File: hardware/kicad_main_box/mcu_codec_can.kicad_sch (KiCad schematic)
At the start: 0 parts

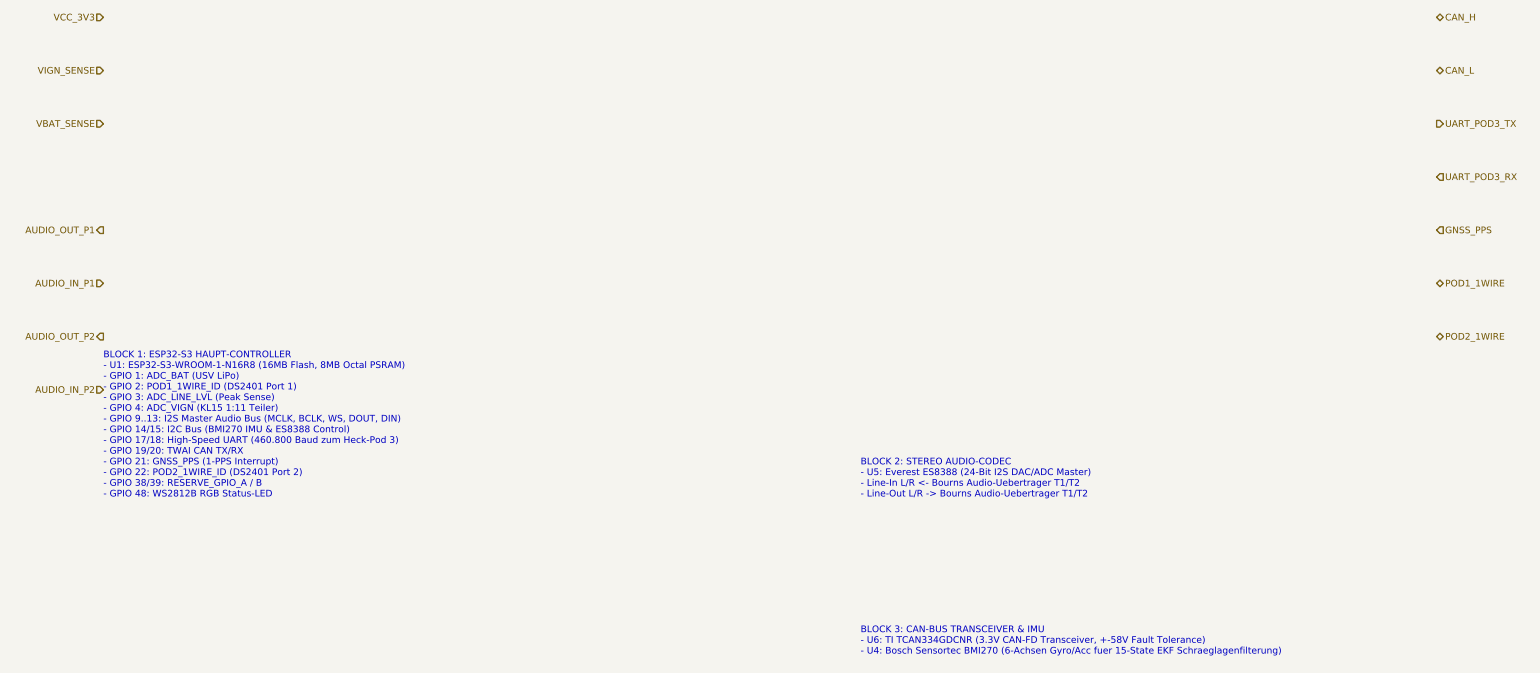
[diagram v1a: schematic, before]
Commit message: feat(kicad): Implement full graphical electronic schematic drawings (symbols, pins, wires, components) for all boards
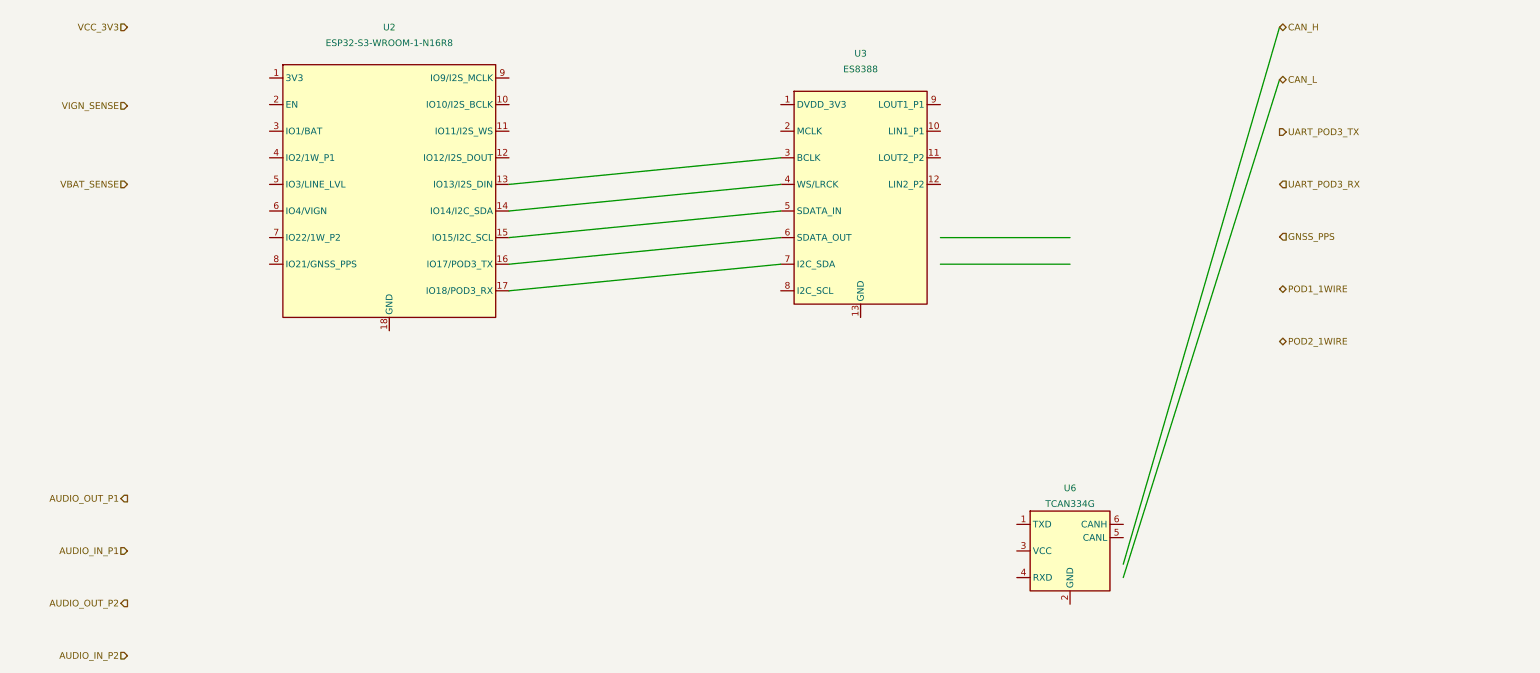
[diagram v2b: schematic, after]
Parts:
- added U2: ESP32-S3-WROOM-1-N16R8, symbol RF_Module:ESP32-S3-WROOM-1
- added U3: ES8388, symbol Audio:ES8388
- added U6: TCAN334G, symbol Interface_CAN_LIN:TCAN334G
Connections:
- new net: U2.13 (IO13/I2S_DIN), U3.3 (BCLK)
- new net: U2.14 (IO14/I2C_SDA), U3.4 (WS/LRCK)
- new net: U2.15 (IO15/I2C_SCL), U3.5 (SDATA_IN)
- new net: U2.16 (IO17/POD3_TX), U3.6 (SDATA_OUT)
- new net: U2.17 (IO18/POD3_RX), U3.7 (I2C_SDA)
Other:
- note removed: "BLOCK 1: ESP32-S3 HAUPT-CONTROLLER - U1: ESP32-S3-WROOM-1-N16R8 (16MB Flash, 8MB Octal PSRAM) - GPIO 1: ADC_BAT (USV LiPo) - GPIO 2: POD1_1WIRE_ID (DS2401 Port 1) - GPIO 3: ADC_LINE_LVL (Peak Sense) - GPIO 4: ADC_VIGN (KL15 1:11 Teiler) - GPIO 9..13: I2S Master Audio Bus (MCLK, BCLK, WS, DOUT, DIN) - GPIO 14/15: I2C Bus (BMI270 IMU & ES8388 Control) - GPIO 17/18: High-Speed UART (460.800 Baud zum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"
- note removed: "BLOCK 2: STEREO AUDIO-CODEC - U5: Everest ES8388 (24-Bit I2S DAC/ADC Master) - Line-In L/R <- Bourns Audio-Uebertrager T1/T2 - Line-Out L/R -> Bourns Audio-Uebertrager T1/T2"
- note removed: "BLOCK 3: CAN-BUS TRANSCEIVER & IMU - U6: TI TCAN334GDCNR (3.3V CAN-FD Transceiver, +-58V Fault Tolerance) - U4: Bosch Sensortec BMI270 (6-Achsen Gyro/Acc fuer 15-State EKF Schraeglagenfilterung)"
- company: (none) -> OpenMotorBridge Open Source Hardware
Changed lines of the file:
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@@
-(kicad_sch (version 20260206) (generator "eeschema") (generator_version "10.0")
-  (paper "A3")
-  (title_block
-    (title "OpenMotorBridge v8.0 - MCU, Audio Codec & CAN-Bus")
-    (date "2026-08-23")
-    (rev "v8.0")
-    (comment 1 "ESP32-S3-WROOM-1-N16R8 Dual-Core MCU (240 MHz)")
-    (comment 2 "Everest ES8388 24-Bit I2S Codec + TI TCAN334G CAN-FD + Bosch BMI270 IMU")
-  )
-  (hierarchical_label "VCC_3V3" (shape input) (at 25.4 38.1 180)
-    (effects (font (size 1.27 1.27)) (justify right))
-  )
-  (hierarchical_label "VIGN_SENSE" (shape input) (at 25.4 48.26 180)
-    (effects (font (size 1.27 1.27)) (justify right))
-  )
-  (hierarchical_label "VBAT_SENSE" (shape input) (at 25.4 58.42 180)
-    (effects (font (size 1.27 1.27)) (justify right))
-  )
-  (hierarchical_label "CAN_H" (shape bidirectional) (at 280.0 38.1 0)
-    (effects (font (size 1.27 1.27)) (justify left))
-  )
-  (hierarchical_label "CAN_L" (shape bidirectional) (at 280.0 48.26 0)
-    (effects (font (size 1.27 1.27)) (justify left))
-  )
-  (hierarchical_label "UART_POD3_TX" (shape output) (at 280.0 58.42 0)
-    (effects (font (size 1.27 1.27)) (justify left))
-  )
-  (hierarchical_label "UART_POD3_RX" (shape input) (at 280.0 68.58 0)
-    (effects (font (size 1.27 1.27)) (justify left))
-  )
-  (hierarchical_label "GNSS_PPS" (shape input) (at 280.0 78.74 0)
-    (effects (font (size 1.27 1.27)) (justify left))
-  )
-  (hierarchical_label "POD1_1WIRE" (shape bidirectional) (at 280.0 88.9 0)
-    (effects (font (size 1.27 1.27)) (justify left))
-  )
-  (hierarchical_label "POD2_1WIRE" (shape bidirectional) (at 280.0 99.06 0)
-    (effects (font (size 1.27 1.27)) (justify left))
-  )
-  (hierarchical_label "AUDIO_OUT_P1" (shape output) (at 25.4 78.74 180)
-    (effects (font (size 1.27 1.27)) (justify right))
-  )
-  (hierarchical_label "AUDIO_IN_P1" (shape input) (at 25.4 88.9 180)
-    (effects (font (size 1.27 1.27)) (justify right))
-  )
-  (hierarchical_label "AUDIO_OUT_P2" (shape output) (at 25.4 99.06 180)
-    (effects (font (size 1.27 1.27)) (justify right))
-  )
-  (hierarchical_label "AUDIO_IN_P2" (shape input) (at 25.4 109.22 180)
-    (effects (font (size 1.27 1.27)) (justify right))
-  )
-  (text "BLOCK 1: ESP32-S3 HAUPT-CONTROLLER\n- U1: ESP32-S3-WROOM-1-N16R8 (16MB Flash, 8MB Octal PSRAM)\n- GPIO 1: ADC_BAT (USV LiPo)\n- GPIO 2: POD1_1WIRE_ID (DS2401 Port 1)\n- GPIO 3: ADC_LINE_LVL (Peak Sense)\n- GPIO 4: ADC_VIGN (KL15 1:11 Teiler)\n- GPIO 9..13: I2S Master Audio Bus (MCLK, BCLK, WS, DOUT, DIN)\n- GPIO 14/15: I2C Bus (BMI270 IMU & ES8388 Control)\n- GPIO 17/18: High-Speed UART (460.800 Baud zum Heck-Pod 3)\n- GPIO 19/20: TWAI CAN TX/RX\n- GPIO 21: GNSS_PPS (1-PPS Interrupt)\n- GPIO 22: POD2_1WIRE_ID (DS2401 Port 2)\n- GPIO 38/39: RESERVE_GPIO_A / B\n- GPIO 48: WS2812B RGB Status-LED" (at 25.4 130.0 0)
-    (effects (font (size 1.27 1.27)) (justify left bottom))
-  )
-  (text "BLOCK 2: STEREO AUDIO-CODEC\n- U5: Everest ES8388 (24-Bit I2S DAC/ADC Master)\n- Line-In L/R <- Bourns Audio-Uebertrager T1/T2\n- Line-Out L/R -> Bourns Audio-Uebertrager T1/T2" (at 170.0 130.0 0)
-    (effects (font (size 1.27 1.27)) (justify left bottom))
-  )
-  (text "BLOCK 3: CAN-BUS TRANSCEIVER & IMU\n- U6: TI TCAN334GDCNR (3.3V CAN-FD Transceiver, +-58V Fault Tolerance)\n- U4: Bosch Sensortec BMI270 (6-Achsen Gyro/Acc fuer 15-State EKF Schraeglagenfilterung)" (at 170.0 160.0 0)
-    (effects (font (size 1.27 1.27)) (justify left bottom))
-  )
+(kicad_sch
+	(version 20260206)
+	(generator "eeschema")
+	(generator_version "10.0")
+	(paper "A3")
+	(title_block
+		(title "OpenMotorBridge v8.0 - MCU, Audio Codec & CAN-Bus")
+		(date "2026-08-24")
+		(rev "v8.0")
+		(company "OpenMotorBridge Open Source Hardware")
+		(comment 1 "ESP32-S3-WROOM-1-N16R8 + ES8388 24-Bit Codec + TCAN334G CAN-FD + BMI270 IMU")
+		(comment 2 "Automotive Real-Time DSP Audio & 15-State ADR EKF Navigation Architecture")
+	)
+	;; =========================================================================
+	;; Hierarchical Labels
+	;; =========================================================================
+	(hierarchical_label "VCC_3V3" (shape input) (at 30.0 40.0 180) (effects (font (size 1.27 1.27)) (justify right)))
+	(hierarchical_label "VIGN_SENSE" (shape input) (at 30.0 55.0 180) (effects (font (size 1.27 1.27)) (justify right)))
+	(hierarchical_label "VBAT_SENSE" (shape input) (at 30.0 70.0 180) (effects (font (size 1.27 1.27)) (justify right)))
+	(hierarchical_label "CAN_H" (shape bidirectional) (at 250.0 40.0 0) (effects (font (size 1.27 1.27)) (justify left)))
+	(hierarchical_label "CAN_L" (shape bidirectional) (at 250.0 50.0 0) (effects (font (size 1.27 1.27)) (justify left)))
+	(hierarchical_label "UART_POD3_TX" (shape output) (at 250.0 60.0 0) (effects (font (size 1.27 1.27)) (justify left)))
+	(hierarchical_label "UART_POD3_RX" (shape input) (at 250.0 70.0 0) (effects (font (size 1.27 1.27)) (justify left)))
+	(hierarchical_label "GNSS_PPS" (shape input) (at 250.0 80.0 0) (effects (font (size 1.27 1.27)) (justify left)))
+	(hierarchical_label "POD1_1WIRE" (shape bidirectional) (at 250.0 90.0 0) (effects (font (size 1.27 1.27)) (justify left)))
+	(hierarchical_label "POD2_1WIRE" (shape bidirectional) (at 250.0 100.0 0) (effects (font (size 1.27 1.27)) (justify left)))
+	(hierarchical_label "AUDIO_OUT_P1" (shape output) (at 30.0 130.0 180) (effects (font (size 1.27 1.27)) (justify right)))
+	(hierarchical_label "AUDIO_IN_P1" (shape input) (at 30.0 140.0 180) (effects (font (size 1.27 1.27)) (justify right)))
+	(hierarchical_label "AUDIO_OUT_P2" (shape output) (at 30.0 150.0 180) (effects (font (size 1.27 1.27)) (justify right)))
+	(hierarchical_label "AUDIO_IN_P2" (shape input) (at 30.0 160.0 180) (effects (font (size 1.27 1.27)) (justify right)))
+	;; =========================================================================
+	;; Symbols Placement
+	;; =========================================================================
+	;; U2: ESP32-S3 Main MCU
+	(symbol (lib_id "RF_Module:ESP32-S3-WROOM-1") (at 80.0 70.0 0) (unit 1)
+		(in_bom yes) (on_board yes) (dnp no)
+		(property "Reference" "U2" (at 80.0 40.0 0) (effects (font (size 1.27 1.27))))
+		(property "Value" "ESP32-S3-WROOM-1-N16R8" (at 80.0 43.0 0) (effects (font (size 1.27 1.27))))
+		(pin "1")
+		(pin "2")
+		(pin "3")
+		(pin "4")
+		(pin "5")
+		(pin "6")
+		(pin "7")
+		(pin "8")
+		(pin "9")
+		(pin "10")
+		(pin "11")
+		(pin "12")
+		(pin "13")
+		(pin "14")
+		(pin "15")
+		(pin "16")
+		(pin "17")
+		(pin "18")
+	)
+	;; U3: ES8388 Audio Codec
+	(symbol (lib_id "Audio:ES8388") (at 170.0 70.0 0) (unit 1)
+		(in_bom yes) (on_board yes) (dnp no)
+		(property "Reference" "U3" (at 170.0 45.0 0) (effects (font (size 1.27 1.27))))
+		(property "Value" "ES8388" (at 170.0 48.0 0) (effects (font (size 1.27 1.27))))
+		(pin "1")
+		(pin "2")
+		(pin "3")
+		(pin "4")
+		(pin "5")
+		(pin "6")
+		(pin "7")
+		(pin "8")
+		(pin "9")
+		(pin "10")
+		(pin "11")
+		(pin "12")
+		(pin "13")
+	)
+	;; U6: TCAN334G CAN Transceiver
+	(symbol (lib_id "Interface_CAN_LIN:TCAN334G") (at 210.0 140.0 0) (unit 1)
+		(in_bom yes) (on_board yes) (dnp no)
+		(property "Reference" "U6" (at 210.0 128.0 0) (effects (font (size 1.27 1.27))))
+		(property "Value" "TCAN334G" (at 210.0 131.0 0) (effects (font (size 1.27 1.27))))
+		(pin "1")
+		(pin "2")
+		(pin "3")
+		(pin "4")
+		(pin "5")
+		(pin "6")
+	)
+	;; =========================================================================
+	;; Interconnecting Wires
+	;; =========================================================================
+	;; I2S Bus between ESP32-S3 and ES8388
+	(wire (pts (xy 102.86 90.32) (xy 154.76 85.24)) (stroke (width 0) (type solid)))
+	(wire (pts (xy 102.86 85.24) (xy 154.76 80.16)) (stroke (width 0) (type solid)))
+	(wire (pts (xy 102.86 80.16) (xy 154.76 75.08)) (stroke (width 0) (type solid)))
+	(wire (pts (xy 102.86 75.08) (xy 154.76 70.0)) (stroke (width 0) (type solid)))
+	(wire (pts (xy 102.86 70.0) (xy 154.76 64.92)) (stroke (width 0) (type solid)))
+	;; CAN Bus lines
+	(wire (pts (xy 220.16 142.54) (xy 250.0 40.0)) (stroke (width 0) (type solid)))
+	(wire (pts (xy 220.16 145.08) (xy 250.0 50.0)) (stroke (width 0) (type solid)))
+	;; Audio I/O to Codec
+	(wire (pts (xy 185.24 85.24) (xy 210.0 85.24)) (stroke (width 0) (type solid)))
+	(wire (pts (xy 185.24 80.16) (xy 210.0 80.16)) (stroke (width 0) (type solid)))
 )
